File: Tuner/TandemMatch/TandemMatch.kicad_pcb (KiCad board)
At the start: 2 copper layers, 100 x 100 mm, 122 parts, among them J1 Conn_01x02, J10 Conn_01x01, J11 Conn_01x01, J12 Conn_01x01, J13 Conn_01x01, J14 Conn_01x01, J15 Conn_01x01, J16 Conn_01x01, J17 Conn_01x02, J18 Conn_Coaxial, J19 Conn_01x02, J2 Conn_01x02, J20 Conn_Coaxial, J21 Conn_01x01, J22 Conn_01x01, J23 Conn_01x01, J24 Conn_01x01, J25 Conn_01x01, J26 Conn_01x01, J27 Conn_01x01, J28 Conn_01x01, J29 Conn_01x01, J3 Conn_Coaxial, J30 Conn_01x01, J31 Conn_01x01, J32 Conn_01x01, J33 Conn_01x03, J34 Conn_01x01, J35 Conn_01x01, J36 Conn_01x01, J37 Conn_01x01, J38 Conn_01x01, J39 Conn_01x01, J4 Conn_Coaxial, J40 Conn_01x01, J41 Conn_01x01, J42 Conn_01x01, J43 Conn_01x02, J44 Conn_Coaxial, J45 Conn_01x01, J46 Conn_01x01, J47 Conn_01x01, J48 Conn_01x01, J49 Conn_01x01, J5 Conn_01x01, J50 Conn_01x01, J51 Conn_01x01, J52 Conn_01x01, J53 Conn_01x01, J54 Conn_01x02, J55 Conn_01x01, J56 Conn_01x01, J57 Conn_01x01, J58 Conn_01x02, J59 Conn_Coaxial, J6 Conn_01x01, J60 Conn_01x01, J61 Conn_01x01, J62 Conn_01x01, J63 Conn_01x01, J64 Conn_01x01, J65 Conn_01x01, J66 Conn_01x01, J67 Conn_01x01, J68 Conn_01x02, J69 Conn_01x01, J7 Conn_01x01, J70 Conn_01x01, J71 Conn_01x01, J72 Conn_01x01, J73 Conn_01x02, J74 Conn_01x02, J75 Conn_01x02, J76 Conn_01x02, J77 Conn_01x01, J78 Conn_01x01, J79 Conn_01x01, J8 Conn_01x01, J80 Conn_01x01, J81 Conn_01x01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

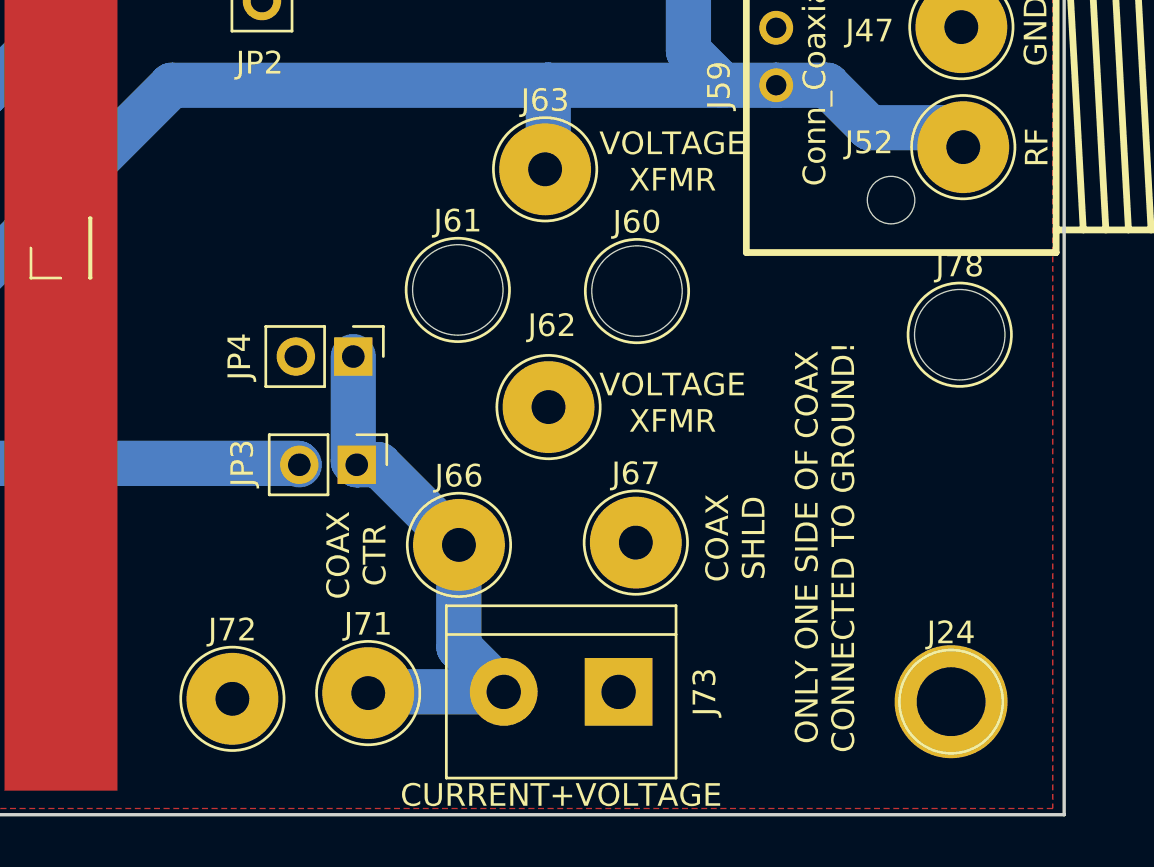
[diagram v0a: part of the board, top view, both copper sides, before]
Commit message: TandemMatch to JLCPCB
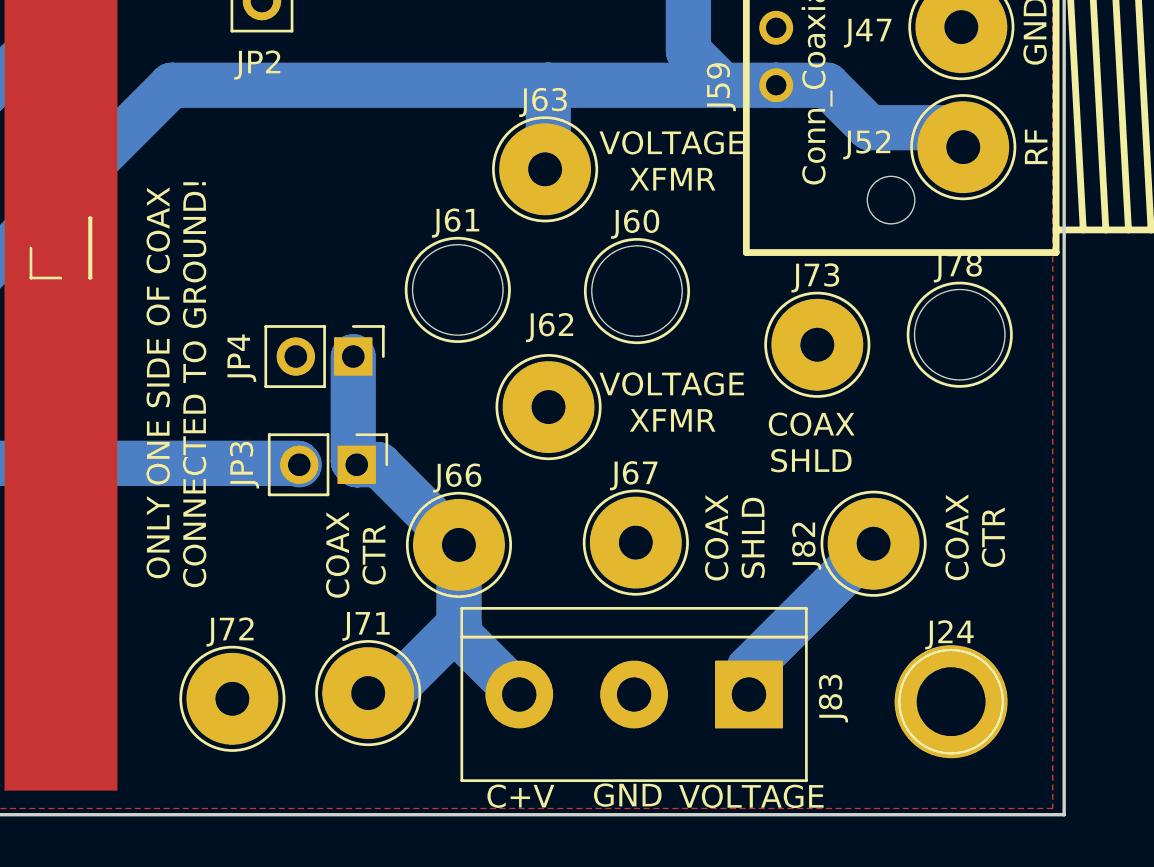
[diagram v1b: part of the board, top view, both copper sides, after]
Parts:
- added J82: Conn_01x01, Connectors:1pin, F.Cu at (131.6, 128.0)
- added J83: Conn_01x03, Connectors_Terminal_Blocks:TerminalBlock_bornier-3_P5.08mm, F.Cu at (126.1, 134.7)
- J73: value Conn_01x02 -> Conn_01x01; footprint Connectors_Terminal_Blocks:TerminalBlock_bornier-2_P5.08mm -> Connectors:1pin
- moved J73 17.7 mm to (129.1, 119.2), turned to 0 degrees
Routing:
- net Net-(J82-Pad1): track 0.00 -> 8.95 mm
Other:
- board text added: "C+V"
- board text removed: "CURRENT+VOLTAGE"
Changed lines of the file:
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@@
 (kicad_pcb (version 4) (host pcbnew 4.0.7)
   (general
-    (links 147)
+    (links 149)
     (no_connects 0)
-    (area 39.924999 39.924999 140.075001 140.075001)
+    (area 18.581999 37.92438 161.377001 141.821259)
     (thickness 1.6)
-    (drawings 61)
-    (tracks 200)
+    (drawings 65)
+    (tracks 204)
     (zones 0)
-    (modules 122)
-    (nets 24)
+    (modules 124)
+    (nets 25)
   )
   (page A4)
@@
     (mod_text_size 1 1)
     (mod_text_width 0.15)
-    (pad_size 4 4)
-    (pad_drill 4)
+    (pad_size 4.064 4.064)
+    (pad_drill 1.5)
     (pad_to_mask_clearance 0.2)
     (aux_axis_origin 0 0)
@@
   (net 22 "Net-(C10-Pad1)")
   (net 23 "Net-(D5-Pad2)")
+  (net 24 "Net-(J82-Pad1)")
   (net_class Default "This is the default net class."
     (clearance 0.2)
@@
     (add_net "Net-(J52-Pad1)")
     (add_net "Net-(J66-Pad1)")
+    (add_net "Net-(J82-Pad1)")
   )
   (module Connectors_Terminal_Blocks:TerminalBlock_bornier-2_P5.08mm (layer F.Cu)
@@
       (net 2 GND))
   )
-  (module Connectors_Terminal_Blocks:TerminalBlock_bornier-2_P5.08mm (layer F.Cu)
-    (at 120.2944 134.5692 180)
-    (descr "simple 2-pin terminal block, pitch 5.08mm, revamped version of bornier2")
-    (tags "terminal block bornier2")
-    (fp_text reference J73 (at -3.81 0 270) (layer F.SilkS)
-      (effects (font (size 1 1) (thickness 0.15)))
-    )
-    (fp_text value Conn_01x02 (at 2.54 5.08 180) (layer F.Fab)
-      (effects (font (size 1 1) (thickness 0.15)))
-    )
-    (fp_text user %R (at 2.54 0 180) (layer F.Fab)
-      (effects (font (size 1 1) (thickness 0.15)))
-    )
-    (fp_line (start -2.41 2.55) (end 7.49 2.55) (layer F.Fab) (width 0.1))
-    (fp_line (start -2.46 -3.75) (end -2.46 3.75) (layer F.Fab) (width 0.1))
-    (fp_line (start -2.46 3.75) (end 7.54 3.75) (layer F.Fab) (width 0.1))
-    (fp_line (start 7.54 3.75) (end 7.54 -3.75) (layer F.Fab) (width 0.1))
-    (fp_line (start 7.54 -3.75) (end -2.46 -3.75) (layer F.Fab) (width 0.1))
-    (fp_line (start 7.62 2.54) (end -2.54 2.54) (layer F.SilkS) (width 0.12))
-    (fp_line (start 7.62 3.81) (end 7.62 -3.81) (layer F.SilkS) (width 0.12))
-    (fp_line (start 7.62 -3.81) (end -2.54 -3.81) (layer F.SilkS) (width 0.12))
-    (fp_line (start -2.54 -3.81) (end -2.54 3.81) (layer F.SilkS) (width 0.12))
-    (fp_line (start -2.54 3.81) (end 7.62 3.81) (layer F.SilkS) (width 0.12))
-    (fp_line (start -2.71 -4) (end 7.79 -4) (layer F.CrtYd) (width 0.05))
-    (fp_line (start -2.71 -4) (end -2.71 4) (layer F.CrtYd) (width 0.05))
-    (fp_line (start 7.79 4) (end 7.79 -4) (layer F.CrtYd) (width 0.05))
-    (fp_line (start 7.79 4) (end -2.71 4) (layer F.CrtYd) (width 0.05))
-    (pad 1 thru_hole rect (at 0 0 180) (size 3 3) (drill 1.52) (layers *.Cu *.Mask)
-      (net 2 GND))
-    (pad 2 thru_hole circle (at 5.08 0 180) (size 3 3) (drill 1.52) (layers *.Cu *.Mask)
-      (net 14 "Net-(J66-Pad1)"))
-    (model ${KISYS3DMOD}/Terminal_Blocks.3dshapes/TerminalBlock_bornier-2_P5.08mm.wrl
-      (at (xyz 0.1 0 0))
-      (scale (xyz 1 1 1))
-      (rotate (xyz 0 0 0))
-    )
-  )
   (module Pin_Headers:Pin_Header_Straight_1x02_Pitch2.54mm (layer F.Cu)
     (at 104.521 101.473)
@@
     (pad "" np_thru_hole circle (at 0 0 90) (size 4 4) (drill 4) (layers *.Cu *.Mask))
   )
+  (module Connectors:1pin (layer F.Cu)
+    (at 129.0828 119.2149)
+    (descr "module 1 pin (ou trou mecanique de percage)")
+    (tags DEV)
+    (fp_text reference J73 (at 0 -3.048) (layer F.SilkS)
+      (effects (font (size 1 1) (thickness 0.15)))
+    )
+    (fp_text value Conn_01x01 (at 0 3) (layer F.Fab)
+      (effects (font (size 1 1) (thickness 0.15)))
+    )
+    (fp_circle (center 0 0) (end 2 0.8) (layer F.Fab) (width 0.1))
+    (fp_circle (center 0 0) (end 2.6 0) (layer F.CrtYd) (width 0.05))
+    (fp_circle (center 0 0) (end 0 -2.286) (layer F.SilkS) (width 0.12))
+    (pad 1 thru_hole circle (at 0 0) (size 4.064 4.064) (drill 1.5) (layers *.Cu *.Mask)
+      (net 2 GND))
+  )
+  (module Connectors:1pin (layer F.Cu)
+    (at 131.572 128.016 90)
+    (descr "module 1 pin (ou trou mecanique de percage)")
+    (tags DEV)
+    (fp_text reference J82 (at 0 -3.048 90) (layer F.SilkS)
+      (effects (font (size 1 1) (thickness 0.15)))
+    )
+    (fp_text value Conn_01x01 (at 0 3 90) (layer F.Fab)
+      (effects (font (size 1 1) (thickness 0.15)))
+    )
+    (fp_circle (center 0 0) (end 2 0.8) (layer F.Fab) (width 0.1))
+    (fp_circle (center 0 0) (end 2.6 0) (layer F.CrtYd) (width 0.05))
+    (fp_circle (center 0 0) (end 0 -2.286) (layer F.SilkS) (width 0.12))
+    (pad 1 thru_hole circle (at 0 0 90) (size 4.064 4.064) (drill 1.5) (layers *.Cu *.Mask)
+      (net 24 "Net-(J82-Pad1)"))
+  )
+  (module Connectors_Terminal_Blocks:TerminalBlock_bornier-3_P5.08mm (layer F.Cu)
+    (at 126.0602 134.6835 180)
+    (descr "simple 3-pin terminal block, pitch 5.08mm, revamped version of bornier3")
+    (tags "terminal block bornier3")
+    (fp_text reference J83 (at -3.6449 -0.0889 270) (layer F.SilkS)
+      (effects (font (size 1 1) (thickness 0.15)))
+    )
+    (fp_text value Conn_01x03 (at 5.08 5.08 180) (layer F.Fab)
+      (effects (font (size 1 1) (thickness 0.15)))
+    )
+    (fp_text user %R (at 5.08 0 180) (layer F.Fab)
+      (effects (font (size 1 1) (thickness 0.15)))
+    )
+    (fp_line (start -2.47 2.55) (end 12.63 2.55) (layer F.Fab) (width 0.1))
+    (fp_line (start -2.47 -3.75) (end 12.63 -3.75) (layer F.Fab) (width 0.1))
+    (fp_line (start 12.63 -3.75) (end 12.63 3.75) (layer F.Fab) (width 0.1))
+    (fp_line (start 12.63 3.75) (end -2.47 3.75) (layer F.Fab) (width 0.1))
+    (fp_line (start -2.47 3.75) (end -2.47 -3.75) (layer F.Fab) (width 0.1))
+    (fp_line (start -2.54 3.81) (end -2.54 -3.81) (layer F.SilkS) (width 0.12))
+    (fp_line (start 12.7 3.81) (end 12.7 -3.81) (layer F.SilkS) (width 0.12))
+    (fp_line (start -2.54 2.54) (end 12.7 2.54) (layer F.SilkS) (width 0.12))
+    (fp_line (start -2.54 -3.81) (end 12.7 -3.81) (layer F.SilkS) (width 0.12))
+    (fp_line (start -2.54 3.81) (end 12.7 3.81) (layer F.SilkS) (width 0.12))
+    (fp_line (start -2.72 -4) (end 12.88 -4) (layer F.CrtYd) (width 0.05))
+    (fp_line (start -2.72 -4) (end -2.72 4) (layer F.CrtYd) (width 0.05))
+    (fp_line (start 12.88 4) (end 12.88 -4) (layer F.CrtYd) (width 0.05))
+    (fp_line (start 12.88 4) (end -2.72 4) (layer F.CrtYd) (width 0.05))
+    (pad 1 thru_hole rect (at 0 0 180) (size 3 3) (drill 1.52) (layers *.Cu *.Mask)
+      (net 24 "Net-(J82-Pad1)"))
+    (pad 2 thru_hole circle (at 5.08 0 180) (size 3 3) (drill 1.52) (layers *.Cu *.Mask)
+      (net 2 GND))
+    (pad 3 thru_hole circle (at 10.16 0 180) (size 3 3) (drill 1.52) (layers *.Cu *.Mask)
+      (net 14 "Net-(J66-Pad1)"))
+    (model ${KISYS3DMOD}/Terminal_Blocks.3dshapes/TerminalBlock_bornier-3_P5.08mm.wrl
+      (at (xyz 0.2 0 0))
+      (scale (xyz 1 1 1))
+      (rotate (xyz 0 0 0))
+    )
+  )
+  (gr_text GND (at 120.7008 139.16914) (layer F.SilkS)
+    (effects (font (size 1 1) (thickness 0.15)))
+  )
+  (gr_text VOLTAGE (at 126.20498 139.22502) (layer F.SilkS)
+    (effects (font (size 1 1) (thickness 0.15)))
+  )
+  (gr_text "COAX\nCTR" (at 136.1059 127.7493 90) (layer F.SilkS)
+    (effects (font (size 1 1) (thickness 0.15)))
+  )
+  (gr_text "COAX\nSHLD" (at 128.8161 123.571) (layer F.SilkS)
+    (effects (font (size 1 1) (thickness 0.15)))
+  )
   (gr_text GND (at 58.0136 139.1412) (layer F.SilkS)
     (effects (font (size 1 1) (thickness 0.15)))
@@
     (effects (font (size 1 1) (thickness 0.15)))
   )
-  (gr_text CURRENT+VOLTAGE (at 117.7544 139.1412) (layer F.SilkS)
+  (gr_text C+V (at 115.9383 139.2174) (layer F.SilkS)
     (effects (font (size 1 1) (thickness 0.15)))
   )
@@
     (effects (font (size 1 1) (thickness 0.15)))
   )
-  (gr_text "ONLY ONE SIDE OF COAX\nCONNECTED TO GROUND!" (at 129.4384 128.1684 90) (layer F.SilkS)
+  (gr_text "ONLY ONE SIDE OF COAX\nCONNECTED TO GROUND!" (at 100.7745 120.9167 90) (layer F.SilkS)
     (effects (font (size 1 1) (thickness 0.15)))
   )
@@
   (segment (start 129.51714 107.73664) (end 131.3942 109.6137) (width 2) (layer B.Cu) (net 13))
   (segment (start 134.67588 109.6137) (end 135.53694 110.47476) (width 2) (layer B.Cu) (net 13))
+  (segment (start 109.22 134.62) (end 110.2106 134.62) (width 2) (layer B.Cu) (net 14))
+  (segment (start 110.2106 134.62) (end 113.2332 131.5974) (width 2) (layer B.Cu) (net 14))
+  (segment (start 113.2332 128.0668) (end 113.2332 131.5974) (width 2) (layer B.Cu) (net 14))
+  (segment (start 113.2332 131.5974) (end 113.2332 132.0165) (width 2) (layer B.Cu) (net 14))
+  (segment (start 113.2332 132.0165) (end 115.9002 134.6835) (width 2) (layer B.Cu) (net 14))
   (segment (start 108.5596 119.7356) (end 108.5596 124.3711) (width 2) (layer B.Cu) (net 14))
   (segment (start 108.5596 124.3711) (end 108.712 124.5235) (width 2) (layer B.Cu) (net 14))
-  (segment (start 115.2144 134.5692) (end 109.2708 134.5692) (width 2) (layer B.Cu) (net 14))
   (segment (start 109.2708 134.5692) (end 109.22 134.62) (width 2) (layer B.Cu) (net 14))
-  (segment (start 113.2332 128.0668) (end 113.2332 132.588) (width 2) (layer B.Cu) (net 14))
-  (segment (start 113.2332 132.588) (end 115.2144 134.5692) (width 2) (layer B.Cu) (net 14))
   (segment (start 108.712 124.5235) (end 109.6899 124.5235) (width 2) (layer B.Cu) (net 14))
   (segment (start 109.6899 124.5235) (end 113.2332 128.0668) (width 2) (layer B.Cu) (net 14))
@@
   (segment (start 111.76 94.5515) (end 111.887 94.4245) (width 2) (layer B.Cu) (net 23))
   (segment (start 111.76 94.5515) (end 111.887 94.4245) (width 2) (layer B.Cu) (net 23))
+  (segment (start 126.0602 134.6835) (end 126.0602 133.5278) (width 2) (layer B.Cu) (net 24))
+  (segment (start 126.0602 133.5278) (end 131.572 128.016) (width 2) (layer B.Cu) (net 24))
   (zone (net 2) (net_name GND) (layer F.Cu) (hatch edge 0.508)
     (connect_pads (clearance 0.635))
